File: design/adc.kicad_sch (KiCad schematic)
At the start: 27 parts, among them J6 JUMPER_DFS/GAIN, U12 TLV431ACDBZR, U13 AD9214

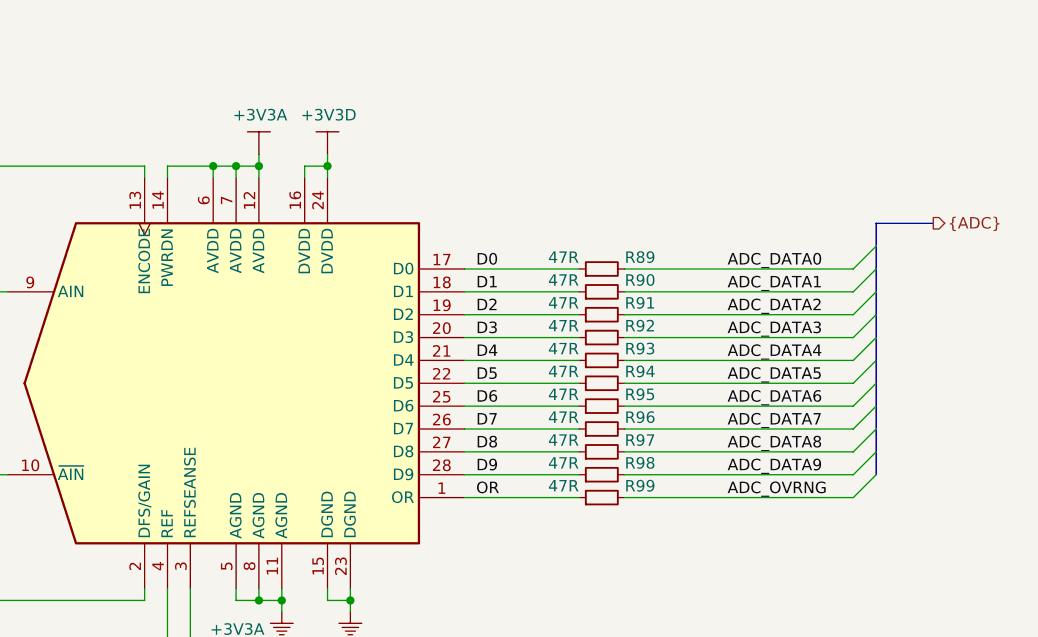
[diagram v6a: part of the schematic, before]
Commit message: Fixed ADC PWRDN problem
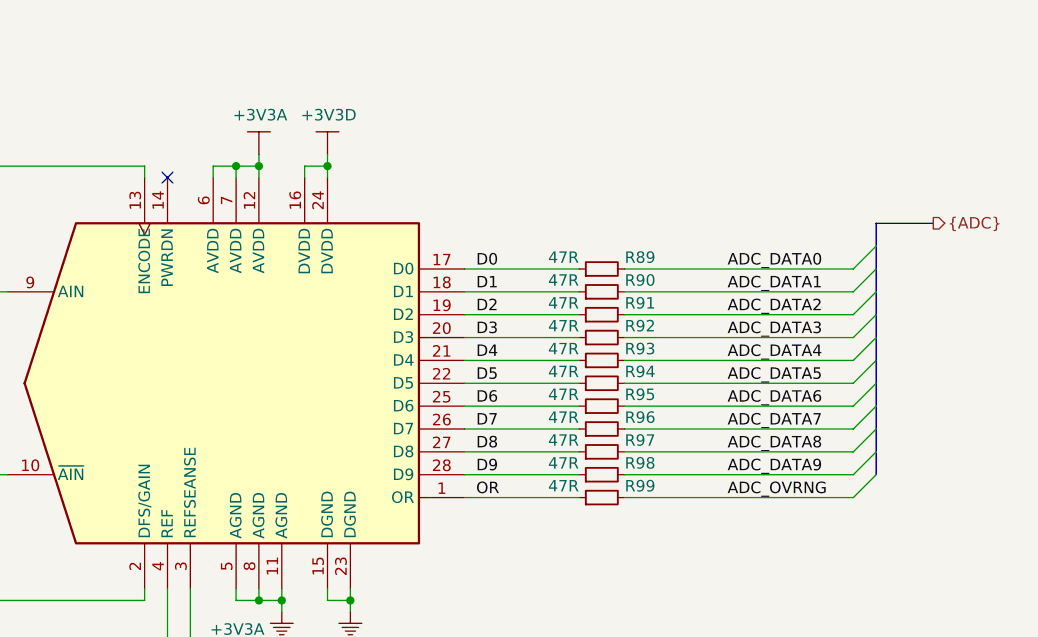
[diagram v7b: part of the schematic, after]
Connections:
- net +3V3A: no longer U13.14 (PWRDN)
- no-connect marks 1 -> 2
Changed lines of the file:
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@@
-(kicad_sch (version 20200608) (host eeschema "5.99.0-unknown-ad69e44~101~ubuntu18.04.1")
+(kicad_sch (version 20200618) (host eeschema "5.99.0-unknown-f420396~101~ubuntu18.04.1")
   (page 7 8)
   (paper "A4")
@@
   )
   (bus_alias "ADC" (members "ADC_DATA[0..9]" "ADC_OVRNG"))
-  (junction (at 29.21 165.1))
-  (junction (at 30.48 24.13))
-  (junction (at 40.64 24.13))
-  (junction (at 49.53 165.1))
-  (junction (at 52.07 24.13))
-  (junction (at 82.55 24.13))
-  (junction (at 93.98 24.13))
-  (junction (at 105.41 24.13))
-  (junction (at 114.3 124.46))
-  (junction (at 114.3 127))
-  (junction (at 114.3 129.54))
-  (junction (at 116.84 24.13))
-  (junction (at 128.27 24.13))
-  (junction (at 139.7 132.08))
-  (junction (at 144.78 76.2))
-  (junction (at 147.32 76.2))
-  (junction (at 149.86 76.2))
-  (junction (at 149.86 124.46))
-  (junction (at 152.4 124.46))
-  (junction (at 157.48 76.2))
-  (junction (at 160.02 124.46))
+  (junction (at 29.21 165.1) (diameter 0) (color 0 0 0 0))
+  (junction (at 30.48 24.13) (diameter 0) (color 0 0 0 0))
+  (junction (at 40.64 24.13) (diameter 0) (color 0 0 0 0))
+  (junction (at 49.53 165.1) (diameter 0) (color 0 0 0 0))
+  (junction (at 52.07 24.13) (diameter 0) (color 0 0 0 0))
+  (junction (at 82.55 24.13) (diameter 0) (color 0 0 0 0))
+  (junction (at 93.98 24.13) (diameter 0) (color 0 0 0 0))
+  (junction (at 105.41 24.13) (diameter 0) (color 0 0 0 0))
+  (junction (at 114.3 124.46) (diameter 0) (color 0 0 0 0))
+  (junction (at 114.3 127) (diameter 0) (color 0 0 0 0))
+  (junction (at 114.3 129.54) (diameter 0) (color 0 0 0 0))
+  (junction (at 116.84 24.13) (diameter 0) (color 0 0 0 0))
+  (junction (at 128.27 24.13) (diameter 0) (color 0 0 0 0))
+  (junction (at 139.7 132.08) (diameter 0) (color 0 0 0 0))
+  (junction (at 147.32 76.2) (diameter 0) (color 0 0 0 0))
+  (junction (at 149.86 76.2) (diameter 0) (color 0 0 0 0))
+  (junction (at 149.86 124.46) (diameter 0) (color 0 0 0 0))
+  (junction (at 152.4 124.46) (diameter 0) (color 0 0 0 0))
+  (junction (at 157.48 76.2) (diameter 0) (color 0 0 0 0))
+  (junction (at 160.02 124.46) (diameter 0) (color 0 0 0 0))
+  (no_connect (at 139.7 77.47))
   (no_connect (at 100.33 132.08))
-  (bus_entry (at 215.9 87.63) (size 2.54 -2.54))
-  (bus_entry (at 215.9 90.17) (size 2.54 -2.54))
-  (bus_entry (at 215.9 92.71) (size 2.54 -2.54))
-  (bus_entry (at 215.9 95.25) (size 2.54 -2.54))
-  (bus_entry (at 215.9 97.79) (size 2.54 -2.54))
-  (bus_entry (at 215.9 100.33) (size 2.54 -2.54))
-  (bus_entry (at 215.9 102.87) (size 2.54 -2.54))
-  (bus_entry (at 215.9 105.41) (size 2.54 -2.54))
-  (bus_entry (at 215.9 107.95) (size 2.54 -2.54))
-  (bus_entry (at 215.9 110.49) (size 2.54 -2.54))
-  (bus_entry (at 215.9 113.03) (size 2.54 -2.54))
+  (bus_entry (at 215.9 87.63) (size 2.54 -2.54)
+    (stroke (width 0.1524) (type solid) (color 0 0 0 0))
+  )
+  (bus_entry (at 215.9 90.17) (size 2.54 -2.54)
+    (stroke (width 0.1524) (type solid) (color 0 0 0 0))
+  )
+  (bus_entry (at 215.9 92.71) (size 2.54 -2.54)
+    (stroke (width 0.1524) (type solid) (color 0 0 0 0))
+  )
+  (bus_entry (at 215.9 95.25) (size 2.54 -2.54)
+    (stroke (width 0.1524) (type solid) (color 0 0 0 0))
+  )
+  (bus_entry (at 215.9 97.79) (size 2.54 -2.54)
+    (stroke (width 0.1524) (type solid) (color 0 0 0 0))
+  )
+  (bus_entry (at 215.9 100.33) (size 2.54 -2.54)
+    (stroke (width 0.1524) (type solid) (color 0 0 0 0))
+  )
+  (bus_entry (at 215.9 102.87) (size 2.54 -2.54)
+    (stroke (width 0.1524) (type solid) (color 0 0 0 0))
+  )
+  (bus_entry (at 215.9 105.41) (size 2.54 -2.54)
+    (stroke (width 0.1524) (type solid) (color 0 0 0 0))
+  )
+  (bus_entry (at 215.9 107.95) (size 2.54 -2.54)
+    (stroke (width 0.1524) (type solid) (color 0 0 0 0))
+  )
+  (bus_entry (at 215.9 110.49) (size 2.54 -2.54)
+    (stroke (width 0.1524) (type solid) (color 0 0 0 0))
+  )
+  (bus_entry (at 215.9 113.03) (size 2.54 -2.54)
+    (stroke (width 0.1524) (type solid) (color 0 0 0 0))
+  )
   (wire (pts (xy 20.32 24.13) (xy 20.32 25.4))
     (stroke (width 0) (type solid) (color 0 0 0 0))
@@
     (stroke (width 0) (type solid) (color 0 0 0 0))
   )
-  (wire (pts (xy 139.7 77.47) (xy 139.7 76.2))
-    (stroke (width 0) (type solid) (color 0 0 0 0))
-  )
   (wire (pts (xy 139.7 123.19) (xy 139.7 132.08))
     (stroke (width 0) (type solid) (color 0 0 0 0))
@@
     (stroke (width 0) (type solid) (color 0 0 0 0))
   )
-  (wire (pts (xy 144.78 76.2) (xy 139.7 76.2))
-    (stroke (width 0) (type solid) (color 0 0 0 0))
-  )
   (wire (pts (xy 144.78 76.2) (xy 147.32 76.2))
     (stroke (width 0) (type solid) (color 0 0 0 0))
@@
     (stroke (width 0) (type solid) (color 0 0 0 0))
   )
-  (bus (pts (xy 218.44 97.79) (xy 218.44 102.87))
-    (stroke (width 0) (type solid) (color 0 0 0 0))
-  )
-  (bus (pts (xy 218.44 102.87) (xy 218.44 107.95))
-    (stroke (width 0) (type solid) (color 0 0 0 0))
-  )
-  (bus (pts (xy 218.44 107.95) (xy 218.44 110.49))
-    (stroke (width 0) (type solid) (color 0 0 0 0))
-  )
+  (bus (pts (xy 218.44 97.79) (xy 218.44 100.33))
+    (stroke (width 0) (type solid) (color 0 0 0 0))
+  )
+  (bus (pts (xy 218.44 100.33) (xy 218.44 105.41))
+    (stroke (width 0) (type solid) (color 0 0 0 0))
+  )
+  (bus (pts (xy 218.44 105.41) (xy 218.44 110.49))
+    (stroke (width 0) (type solid) (color 0 0 0 0))
+  )

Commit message: Added net classes
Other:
- title: Digitizer 10b 105 MSPS with FPGA -> Digitizer 10b 100 MSPS with FPGA
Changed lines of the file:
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@@
-(kicad_sch (version 20200618) (host eeschema "5.99.0-unknown-f420396~101~ubuntu18.04.1")
-  (page 7 8)
+(kicad_sch (version 20200714) (host eeschema "5.99.0-unknown-039b6fd~102~ubuntu18.04.1")
+  (page 1 8)
   (paper "A4")
   (title_block
-    (title "Digitizer 10b 105 MSPS with FPGA")
+    (title "Digitizer 10b 100 MSPS with FPGA")
     (date "2020-03-09")
     (rev "1.0")
@@
   (bus_alias "ADC" (members "ADC_DATA[0..9]" "ADC_OVRNG"))
   (junction (at 29.21 165.1) (diameter 0) (color 0 0 0 0))
-  (junction (at 30.48 24.13) (diameter 0) (color 0 0 0 0))
-  (junction (at 40.64 24.13) (diameter 0) (color 0 0 0 0))
+  (junction (at 30.48 24.13) (diameter 0) (color 255 0 0 1))
+  (junction (at 40.64 24.13) (diameter 0) (color 255 0 0 1))
   (junction (at 49.53 165.1) (diameter 0) (color 0 0 0 0))
-  (junction (at 52.07 24.13) (diameter 0) (color 0 0 0 0))
-  (junction (at 82.55 24.13) (diameter 0) (color 0 0 0 0))
-  (junction (at 93.98 24.13) (diameter 0) (color 0 0 0 0))
-  (junction (at 105.41 24.13) (diameter 0) (color 0 0 0 0))
+  (junction (at 52.07 24.13) (diameter 0) (color 255 0 0 1))
+  (junction (at 82.55 24.13) (diameter 0) (color 255 0 0 1))
+  (junction (at 93.98 24.13) (diameter 0) (color 255 0 0 1))
+  (junction (at 105.41 24.13) (diameter 0) (color 255 0 0 1))
   (junction (at 114.3 124.46) (diameter 0) (color 0 0 0 0))
   (junction (at 114.3 127) (diameter 0) (color 0 0 0 0))
   (junction (at 114.3 129.54) (diameter 0) (color 0 0 0 0))
-  (junction (at 116.84 24.13) (diameter 0) (color 0 0 0 0))
-  (junction (at 128.27 24.13) (diameter 0) (color 0 0 0 0))
+  (junction (at 116.84 24.13) (diameter 0) (color 255 0 0 1))
+  (junction (at 128.27 24.13) (diameter 0) (color 255 0 0 1))
   (junction (at 139.7 132.08) (diameter 0) (color 0 0 0 0))
-  (junction (at 147.32 76.2) (diameter 0) (color 0 0 0 0))
-  (junction (at 149.86 76.2) (diameter 0) (color 0 0 0 0))
-  (junction (at 149.86 124.46) (diameter 0) (color 0 0 0 0))
-  (junction (at 152.4 124.46) (diameter 0) (color 0 0 0 0))
-  (junction (at 157.48 76.2) (diameter 0) (color 0 0 0 0))
-  (junction (at 160.02 124.46) (diameter 0) (color 0 0 0 0))
+  (junction (at 147.32 76.2) (diameter 0) (color 255 0 0 1))
+  (junction (at 149.86 76.2) (diameter 0) (color 255 0 0 1))
+  (junction (at 149.86 124.46) (diameter 0) (color 0 0 255 1))
+  (junction (at 152.4 124.46) (diameter 0) (color 0 0 255 1))
+  (junction (at 157.48 76.2) (diameter 0) (color 255 0 0 1))
+  (junction (at 160.02 124.46) (diameter 0) (color 0 0 255 1))
+  (no_connect (at 100.33 132.08))
   (no_connect (at 139.7 77.47))
-  (no_connect (at 100.33 132.08))
   (bus_entry (at 215.9 87.63) (size 2.54 -2.54)
     (stroke (width 0.1524) (type solid) (color 0 0 0 0))
